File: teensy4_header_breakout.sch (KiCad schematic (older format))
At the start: 3 parts, among them J1 Conn_01x14, J2 Conn_01x14, U1 GND-1

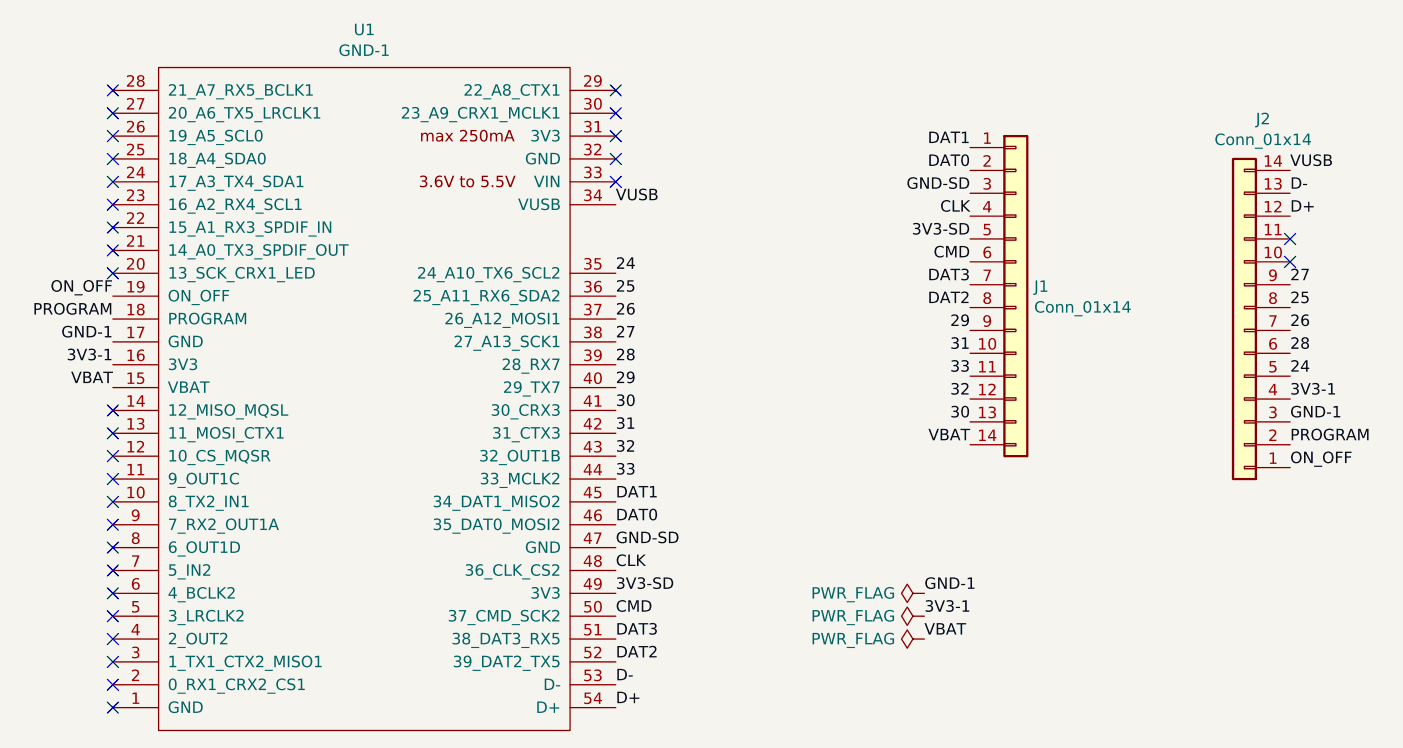
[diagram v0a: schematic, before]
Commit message: Updated two unused pins to GND to allow a basic USB cable to be attached.
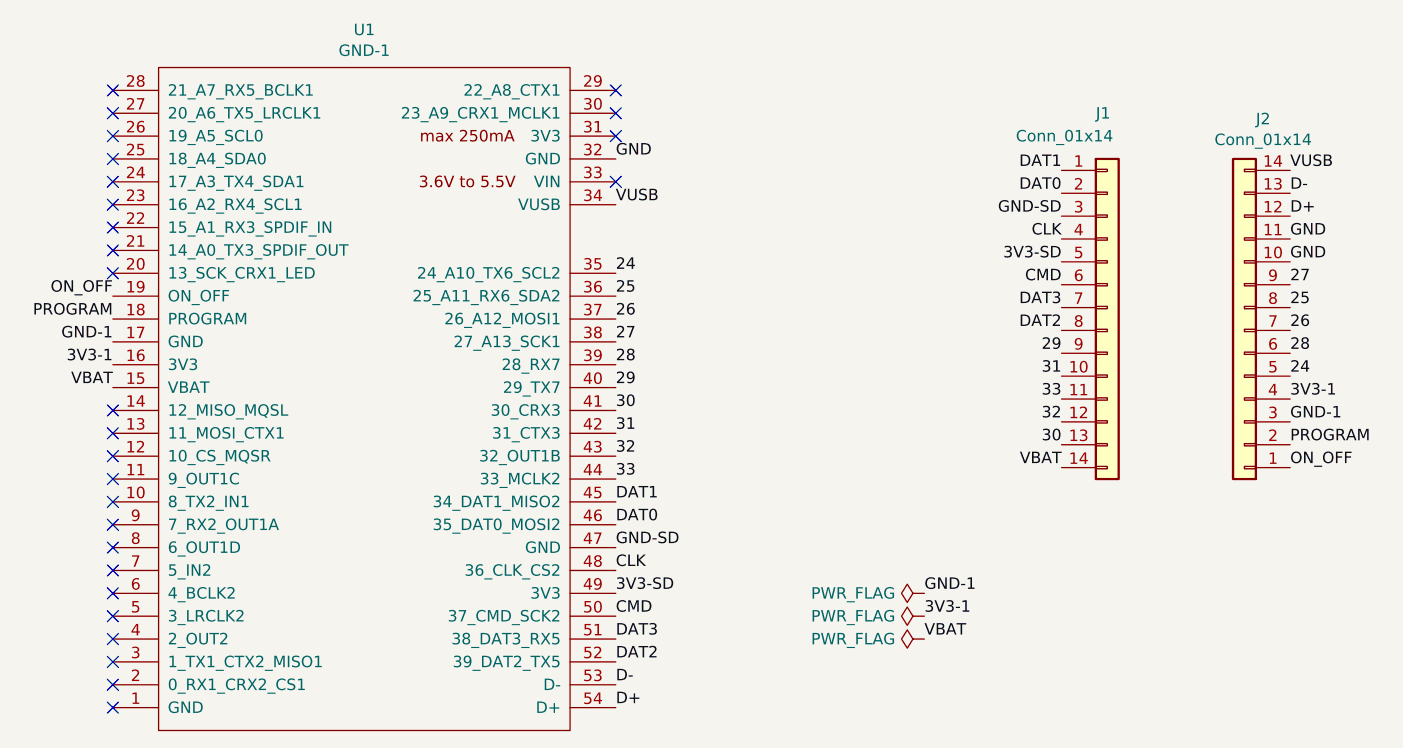
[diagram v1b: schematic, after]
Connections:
- net GND: now reaches U1.32 (GND)
- net GND: now also J2.10 (Pin_10), J2.11 (Pin_11)
- no-connect marks 30 -> 27
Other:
- moved on the sheet: J1
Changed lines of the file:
@@
 EESchema Schematic File Version 4
-EELAYER 29 0
+LIBS:teensy4_header_breakout-cache
+EELAYER 30 0
 EELAYER END
 $Descr A4 11693 8268
@@
 NoConn ~ 4500 3350
 NoConn ~ 6700 3750
-NoConn ~ 6700 3650
 NoConn ~ 6700 3550
 NoConn ~ 6700 3450
@@
 Text Label 6700 5150 0    50   ~ 0
 DAT1
-Text Label 8250 4300 2    50   ~ 0
+Text Label 8650 4400 2    50   ~ 0
 DAT2
-Text Label 8250 4200 2    50   ~ 0
+Text Label 8650 4300 2    50   ~ 0
 DAT3
-Text Label 8250 4100 2    50   ~ 0
+Text Label 8650 4200 2    50   ~ 0
 CMD
-Text Label 8250 3900 2    50   ~ 0
+Text Label 8650 4000 2    50   ~ 0
 CLK
-Text Label 8250 4000 2    50   ~ 0
+Text Label 8650 4100 2    50   ~ 0
 3V3-SD
-Text Label 8250 3800 2    50   ~ 0
+Text Label 8650 3900 2    50   ~ 0
 GND-SD
-Text Label 8250 3700 2    50   ~ 0
+Text Label 8650 3800 2    50   ~ 0
 DAT0
-Text Label 8250 3600 2    50   ~ 0
+Text Label 8650 3700 2    50   ~ 0
 DAT1
-Text Label 8250 4400 2    50   ~ 0
+Text Label 8650 4500 2    50   ~ 0
 29
 $Comp
 L Connector_Generic:Conn_01x14 J1
 U 1 1 5D782E4C
-P 8450 4200
-F 0 "J1" H 8530 4192 50  0000 L CNN
-F 1 "Conn_01x14" H 8530 4101 50  0000 L CNN
-F 2 "Connector_PinHeader_2.54mm:PinHeader_1x14_P2.54mm_Vertical" H 8450 4200 50  0001 C CNN
-F 3 "~" H 8450 4200 50  0001 C CNN
-	1    8450 4200
+P 8850 4300
+F 0 "J1" H 8800 5150 50  0000 L CNN
+F 1 "Conn_01x14" H 8450 5050 50  0000 L CNN
+F 2 "Connector_PinHeader_2.54mm:PinHeader_1x14_P2.54mm_Vertical" H 8850 4300 50  0001 C CNN
+F 3 "~" H 8850 4300 50  0001 C CNN
+	1    8850 4300
 	1    0    0    -1
 $EndComp
-Text Label 8250 4500 2    50   ~ 0
+Text Label 8650 4600 2    50   ~ 0
 31
-Text Label 8250 4600 2    50   ~ 0
+Text Label 8650 4700 2    50   ~ 0
 33
-Text Label 8250 4800 2    50   ~ 0
+Text Label 8650 4900 2    50   ~ 0
 30
-Text Label 8250 4700 2    50   ~ 0
+Text Label 8650 4800 2    50   ~ 0
 32
-Text Label 8250 4900 2    50   ~ 0
+Text Label 8650 5000 2    50   ~ 0
 VBAT
 Text Label 9650 4700 0    50   ~ 0
@@
 Text Label 9650 4300 0    50   ~ 0
 25
-NoConn ~ 9650 4100
-NoConn ~ 9650 4000
 Text Label 6700 5050 0    50   ~ 0
 33
@@
 Text Label 8050 5750 0    50   ~ 0
 VBAT
+Text Label 9650 4000 0    50   ~ 0
+GND
+Text Label 9650 4100 0    50   ~ 0
+GND
+Text Label 6700 3650 0    50   ~ 0
+GND
 $EndSCHEMATC
